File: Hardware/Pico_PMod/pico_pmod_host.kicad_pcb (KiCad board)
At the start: 2 copper layers, 66 x 43.2 mm, 10 parts, among them J1 Conn_02x15_Odd_Even, J2 Conn_01x02, J3 Conn_01x02, J4 Conn_01x02, J5 Conn_01x03, J7 Conn_01x05, SW1 SW_Push, U1 Pico

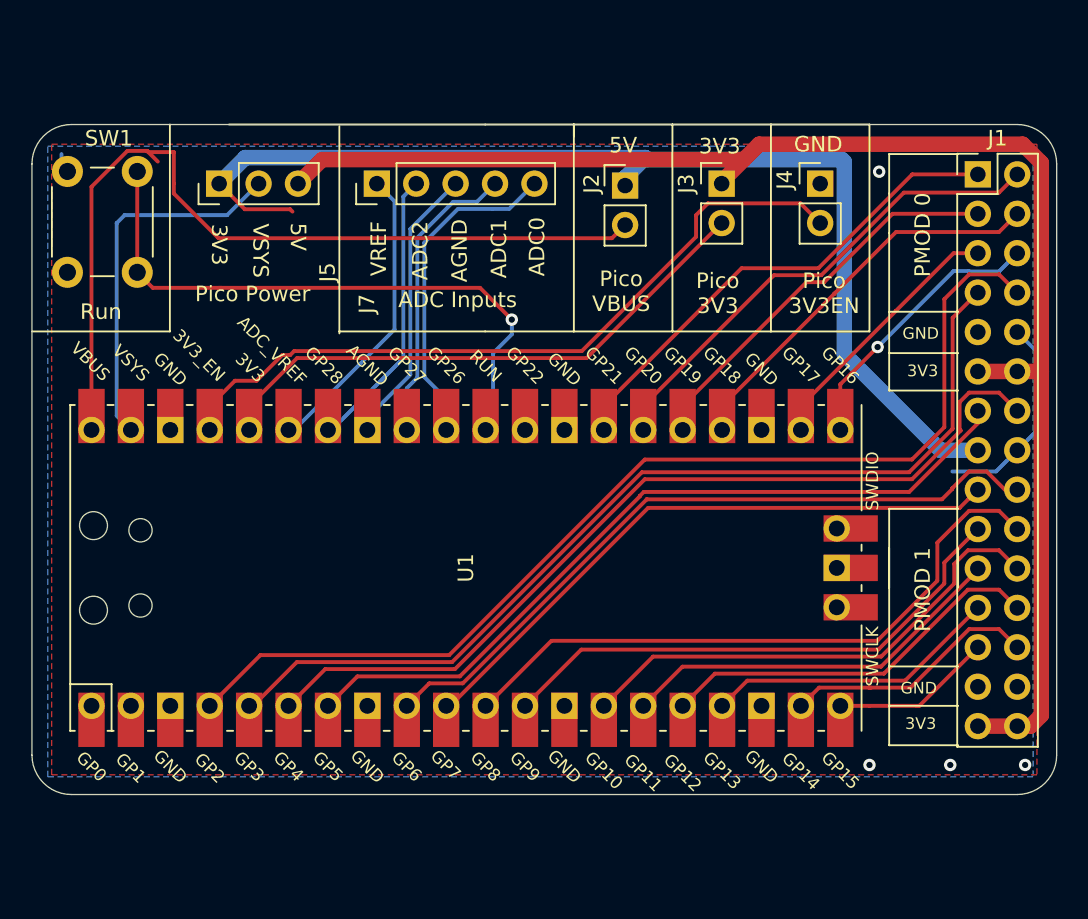
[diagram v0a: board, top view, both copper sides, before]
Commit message: Added mounting holes
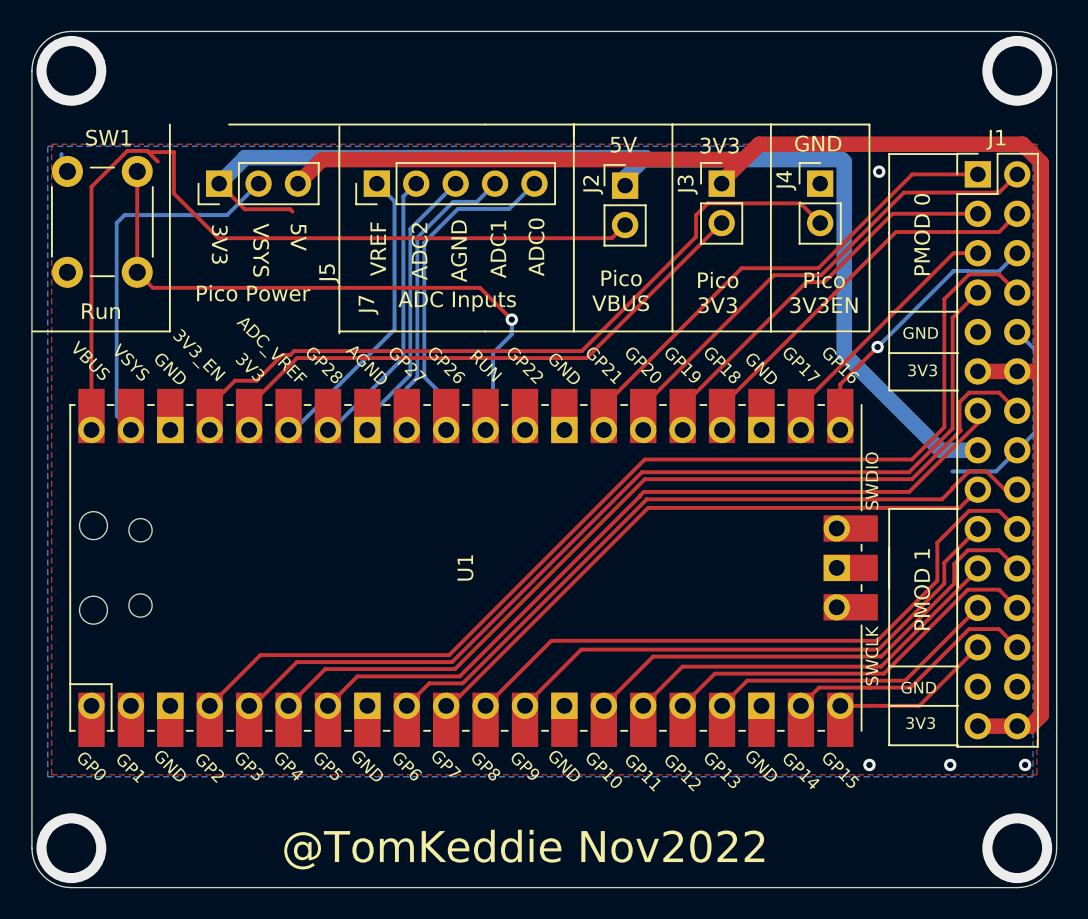
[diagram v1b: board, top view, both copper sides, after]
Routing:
- net (no net): vias 0 -> 4
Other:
- board size 66 x 43.2 mm -> 66 x 55.2 mm
- net class Default removed
- board text added: "@TomKeddie Nov2022"
